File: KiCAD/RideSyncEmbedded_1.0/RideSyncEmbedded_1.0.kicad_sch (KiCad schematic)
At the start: 29 parts, among them IC1 LTC3108, IC2 LTC3108, T1 PA0185NL, U2 LT6106, U3 LT6106, U6 SiP32431DR3, U7 SiP32431DR3

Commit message: 0.1 update
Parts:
- removed C6: 1uF, symbol Device:C
- removed C_store1: 0.1F, symbol Device:C_Polarized_US
- removed IC2: LTC3108, symbol ltc3108-cache:LTC3108
- removed R1: 100ohm/V, symbol Device:R
- removed R3, R6: 5Kohm, symbol Device:R
- removed R4, R5: 50ohm, symbol Device:R
- removed U3: LT6106, Package_TO_SOT_SMD:SOT-23-5, symbol Amplifier_Current:LT6106
- added C_out2: 220uF, symbol Device:C_Polarized_US
- added R2 (x4), R3 (x4): R, symbol Device:R
- added U1: LT6106, Package_TO_SOT_SMD:SOT-23-5, symbol Amplifier_Current:LT6106
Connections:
- net GND: now also C_out2.2, R3.2, R3.2, U1.2 (V-)
- net I_sun: now also R3.2, U1.1
- net I_teg: now also R3.2
- net V_sun: now also SC1.1 (+), C_out2.1, R2.1
- net V_teg: now also R2.1; no longer U2.5 (V+)
- net Vout: now also U2.5 (V+), U1.5 (V+)
- net at U2.3 (-): now also R2.2, R3.1
- net at C4.1, R_sense.2, U6.3 (ON)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: now also R2.1; no longer U2.4 (+)
- net at C5.1, R_sense1.2, U7.3 (ON)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: now also R2.1
- new net: R2.2, R3.1, U2.4 (+)
- new net: R2.2, R3.1, U1.3 (-)
- new net: R2.2, R3.1, U1.4 (+)
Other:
- note added: "MAX40018 | Differential (Grounded) Measurement: VOUT = R3/R2(V1-V2)"
- moved on the sheet: C1, C2, C3, C4, C5, C7, C8, C9, C_out, C_out1, C_store, IC1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

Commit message: schema uodate
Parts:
- removed R_sense, R_sense1: 0.02ohm, symbol Device:R
- added R_sense_LOW (x2): 0.02ohm, symbol Device:R
- added U3, U4: INA190, Package_TO_SOT_SMD:SOT-23, symbol Amplifier_Current1:INA190
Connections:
- net GND: now also R2.1, R2.1, R_sense_LOW.1, R_sense_LOW.1, U3.2 (GND), U3.4 (-), U4.2 (GND), U4.4 (-); no longer C3.2, PE1.1, SC1.2 (-)
- net I_sun: now also U4.1
- net I_teg: now also U3.1
- net V_sun: now also C5.1, U7.3 (ON), U7.4 (IN); no longer R2.1
- net V_teg: now also C3.1, PE1.2, T1.1; no longer C_out.1, IC1.4 (VOUT), R2.1
- net Vout: now also U3.5 (V+), U4.5 (V+)
- net at C4.1, U6.3 (ON), U6.4 (IN): now also C_out.1, IC1.4 (VOUT); no longer R2.1
- new net Sun_sense+: R2.1, R_sense_LOW.2, SC1.2 (-), U4.3 (+)
- new net TEG_sense+: C3.2, PE1.1, R2.1, R_sense_LOW.2, U3.3 (+)
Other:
- note added: "INA190 | Integrated current measurement: - INA190A2: 50 V/V - INA190A3: 100 V/V - INA190A4: 200 V/V"
- note added: "MAX40018 | Discrete current measurement: Differential (Grounded) Measurement: VOUT = R3/R2(V1-V2)"
- note removed: "MAX40018 | Differential (Grounded) Measurement: VOUT = R3/R2(V1-V2)"
- moved on the sheet: C1, C2, C3, C4, C5, C7, C8, C9, C_out, C_out1, C_out2, C_store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

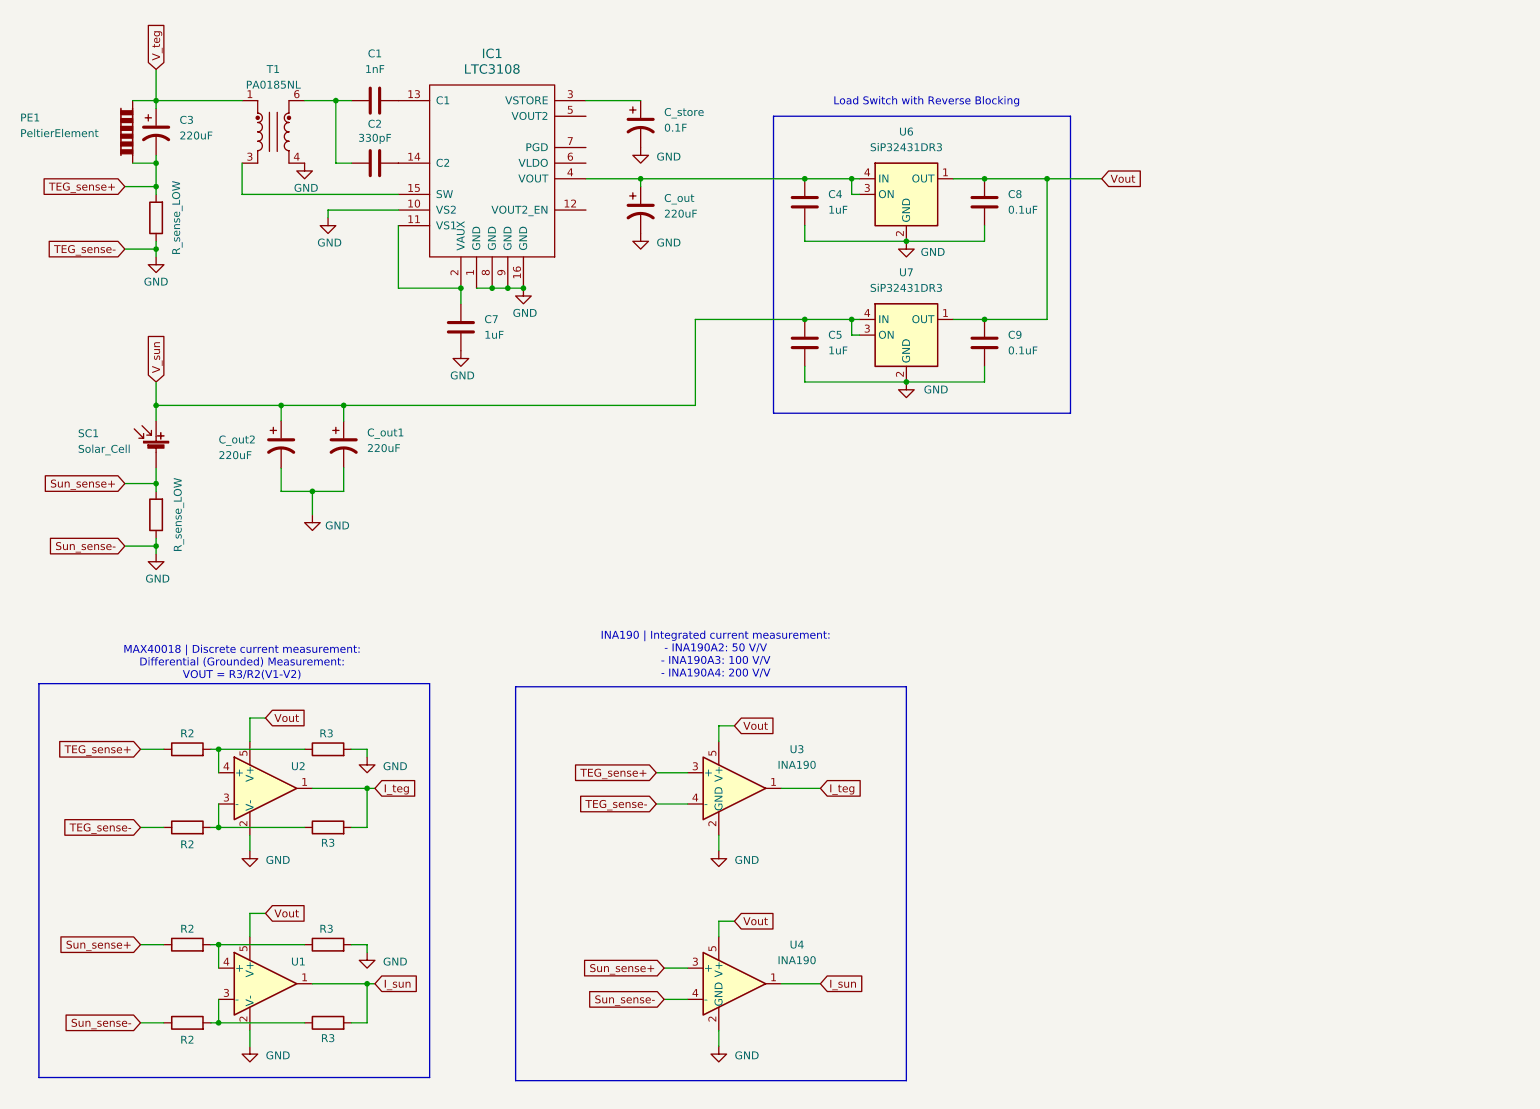
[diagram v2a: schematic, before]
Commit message: voltage buffer added on V-sun, V-teg
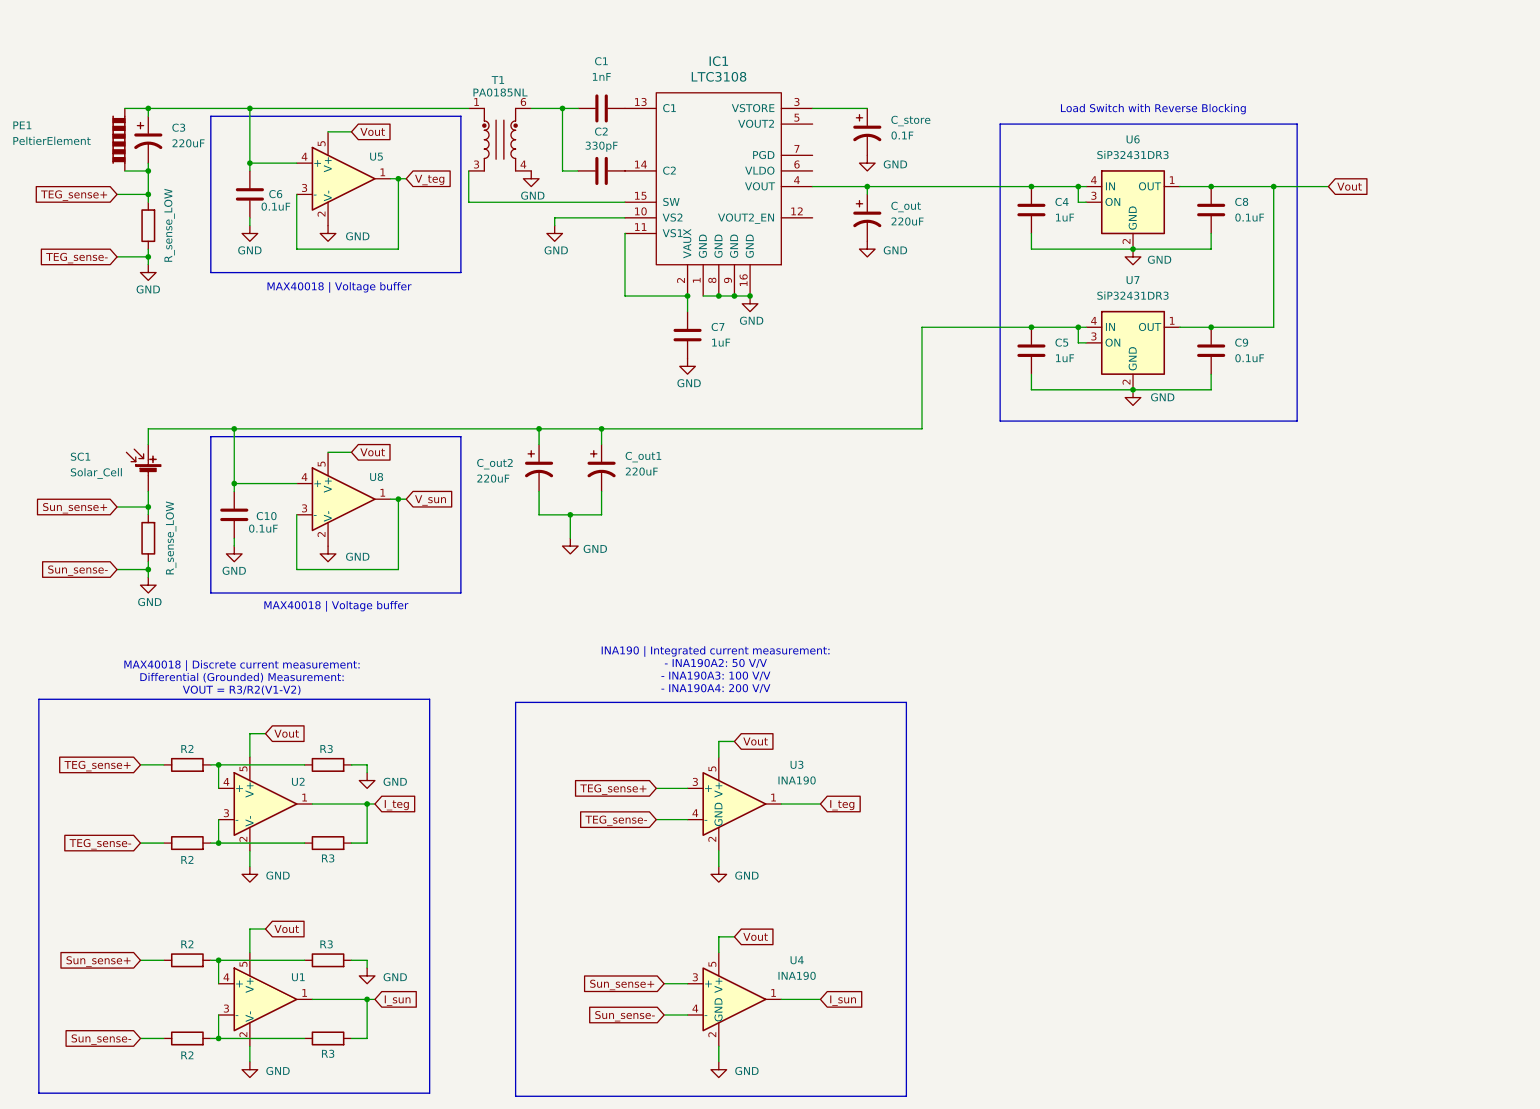
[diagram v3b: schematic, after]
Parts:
- added C10, C6: 0.1uF, symbol Device:C
- added U5, U8: LT6106, Package_TO_SOT_SMD:SOT-23-5, symbol Amplifier_Current:LT6106
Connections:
- net GND: now also C10.2, C6.2, U5.2 (V-), U8.2 (V-)
- net V_sun: now also U8.1, U8.3 (-); no longer C5.1, C_out1.1, C_out2.1, SC1.1 (+), U7.3 (ON), U7.4 (IN)
- net V_teg: now also U5.1, U5.3 (-); no longer C3.1, PE1.2, T1.1
- net Vout: now also U5.5 (V+), U8.5 (V+)
- new net: C3.1, C6.1, PE1.2, T1.1, U5.4 (+)
- new net: C10.1, C5.1, C_out1.1, C_out2.1, SC1.1 (+), U7.3 (ON), U7.4 (IN), U8.4 (+)
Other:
- note added: "MAX40018 | Voltage buffer"
- moved on the sheet: C1, C2, C3, C4, C5, C7, C8, C9, C_out, C_out1, C_out2, C_store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
